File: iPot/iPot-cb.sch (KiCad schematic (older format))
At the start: 60 parts, among them CON1 12VDC, IC1 ATMEGA644-P, IC2 L298, P1 MOT2, P10 I2C3, P11 I2C4, P12 UART, P13 USB_PWR2, P14 ANALOG_IN, P15 PWM_IO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

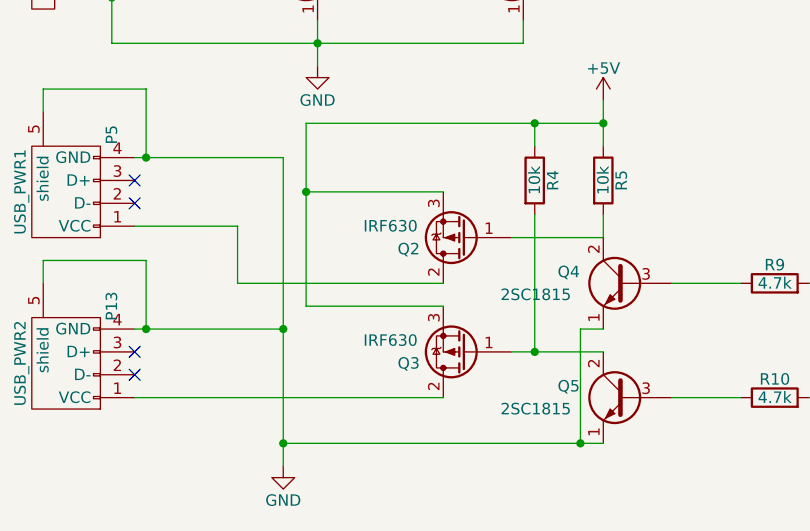
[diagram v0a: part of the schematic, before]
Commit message: Fix MOSFET part No.
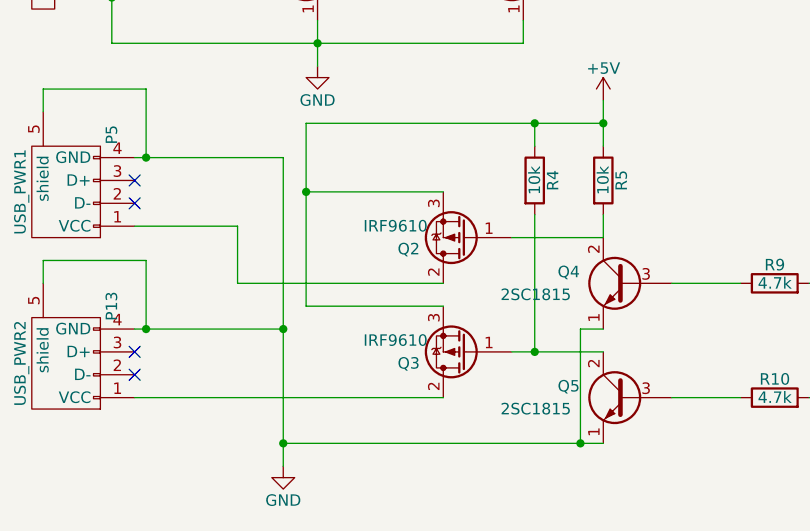
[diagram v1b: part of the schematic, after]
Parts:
- Q2, Q3: value IRF630 -> IRF9610
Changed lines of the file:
@@
 LIBS:lt1376
 LIBS:l298
-LIBS:iPot-cb-cache
 EELAYER 25 0
 EELAYER END
@@
 P 2700 7050
 F 0 "Q3" H 3000 7100 50  0000 R CNN
-F 1 "IRF630" H 3150 7000 50  0000 R CNN
+F 1 "IRF9610" H 3150 7000 50  0000 R CNN
 F 2 "TO_SOT_Packages_THT:TO-220_Neutral123_Vertical" H 2900 7150 50  0001 C CNN
 F 3 "" H 2700 7050 50  0000 C CNN
@@
 P 2700 6550
 F 0 "Q2" H 3000 6600 50  0000 R CNN
-F 1 "IRF630" H 3150 6500 50  0000 R CNN
+F 1 "IRF9610" H 3150 6500 50  0000 R CNN
 F 2 "TO_SOT_Packages_THT:TO-220_Neutral123_Vertical" H 2900 6650 50  0001 C CNN
 F 3 "" H 2700 6550 50  0000 C CNN

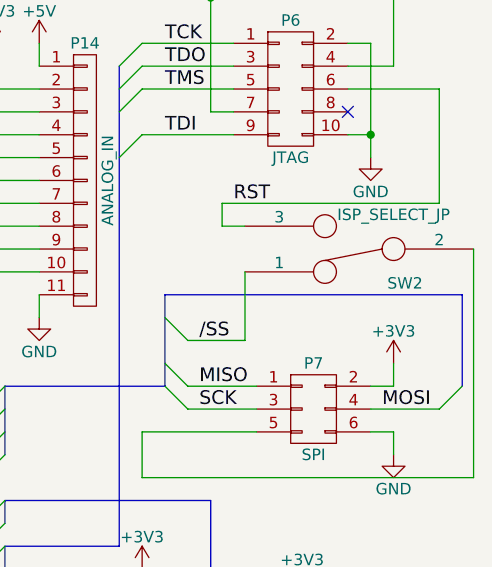
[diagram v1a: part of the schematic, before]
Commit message: Fix possible problems, bump version 1.1
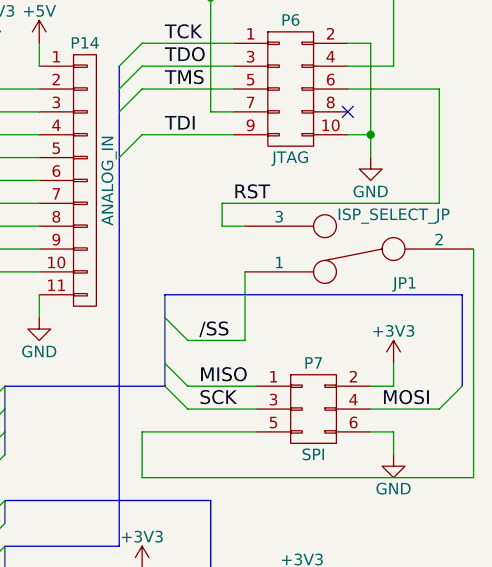
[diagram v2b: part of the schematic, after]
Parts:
- renumbered SW2 to JP1
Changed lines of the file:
@@
 LIBS:lt1376
 LIBS:l298
+LIBS:iPot-cb-cache
 EELAYER 25 0
 EELAYER END
@@
 Title "iPot control board"
 Date "2016-05-04"
-Rev "v1.0"
+Rev "v1.1"
 Comp "Korea University"
 Comment1 "Licensed under CERN OHL v1.2"
@@
 /SS
 $Comp
-L SWITCH_INV SW2
+L SWITCH_INV JP1
 U 1 1 572AF641
 P 10550 1900
-F 0 "SW2" H 10350 2050 50  0000 C CNN
+F 0 "JP1" H 10350 2050 50  0000 C CNN
 F 1 "ISP_SELECT_JP" H 10400 1750 50  0000 C CNN
 F 2 "Pin_Headers:Pin_Header_Straight_1x03" H 10550 1900 50  0001 C CNN

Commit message: Add heatsink
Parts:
- added HS1: HEATSINK, SY403B:SY403B, symbol HEATSINK
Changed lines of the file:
@@
+	1    0    0    -1
+$EndComp
+$Comp
+L HEATSINK HS1
+U 1 1 574BF00C
+P 4150 3150
+F 0 "HS1" H 4150 3350 50  0000 C CNN
+F 1 "HEATSINK" H 4150 3100 50  0000 C CNN
+F 2 "SY403B:SY403B" H 4150 3150 50  0001 C CNN
+F 3 "" H 4150 3150 50  0000 C CNN
+	1    4150 3150
 	1    0    0    -1
 $EndComp

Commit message: Fix bug in silk, fix resistor value, bump version to 1.2
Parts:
- R7: value 270 -> 390
- R8: value 1k -> 680
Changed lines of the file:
@@
 Title "iPot control board"
 Date "2016-05-04"
-Rev "v1.1"
+Rev "v1.2"
 Comp "Korea University"
 Comment1 "Licensed under CERN OHL v1.2"
@@
 P 3000 3250
 F 0 "R8" V 3080 3250 50  0000 C CNN
-F 1 "1k" V 3000 3250 50  0000 C CNN
+F 1 "680" V 3000 3250 50  0000 C CNN
 F 2 "Resistors_ThroughHole:Resistor_Horizontal_RM10mm" V 2930 3250 50  0001 C CNN
 F 3 "" H 3000 3250 50  0000 C CNN
@@
 P 3000 2750
 F 0 "R7" V 3080 2750 50  0000 C CNN
-F 1 "270" V 3000 2750 50  0000 C CNN
+F 1 "390" V 3000 2750 50  0000 C CNN
 F 2 "Resistors_ThroughHole:Resistor_Horizontal_RM10mm" V 2930 2750 50  0001 C CNN
 F 3 "" H 3000 2750 50  0000 C CNN

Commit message: Fix diode footprint
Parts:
- D2: footprint Diodes_ThroughHole:Diode_DO-35_SOD27_Horizontal_RM10 -> Diodes_ThroughHole:Diode_DO-41_SOD81_Horizontal_RM10
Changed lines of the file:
@@
 F 0 "D2" H 1400 1700 50  0000 C CNN
 F 1 "1N5818" H 1400 1500 50  0000 C CNN
-F 2 "Diodes_ThroughHole:Diode_DO-35_SOD27_Horizontal_RM10" H 1400 1600 50  0001 C CNN
+F 2 "Diodes_ThroughHole:Diode_DO-41_SOD81_Horizontal_RM10" H 1400 1600 50  0001 C CNN
 F 3 "" H 1400 1600 50  0000 C CNN
 	1    1400 1600

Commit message: Update
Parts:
- P13, P5: symbol USB_A -> USB_A-RESCUE-iPot-cb
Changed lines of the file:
@@
 EESchema Schematic File Version 2
+LIBS:iPot-cb-rescue
 LIBS:power
 LIBS:device
@@
 $EndComp
 $Comp
-L USB_A P5
+L USB_A-RESCUE-iPot-cb P5
 U 1 1 572727EE
 P 950 6300
@@
 SCL
 $Comp
-L USB_A P13
+L USB_A-RESCUE-iPot-cb P13
 U 1 1 572A937E
 P 950 7050
